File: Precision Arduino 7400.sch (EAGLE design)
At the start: 165 parts, among them U001 74HC4017, U002 74LVC14A, U010 74HC4017, U035 74LVC14A, U101 74HC4017, U110 74HC4017, U201 5319, U401 ATMEGA32U4QFN2, Y401 16MHz

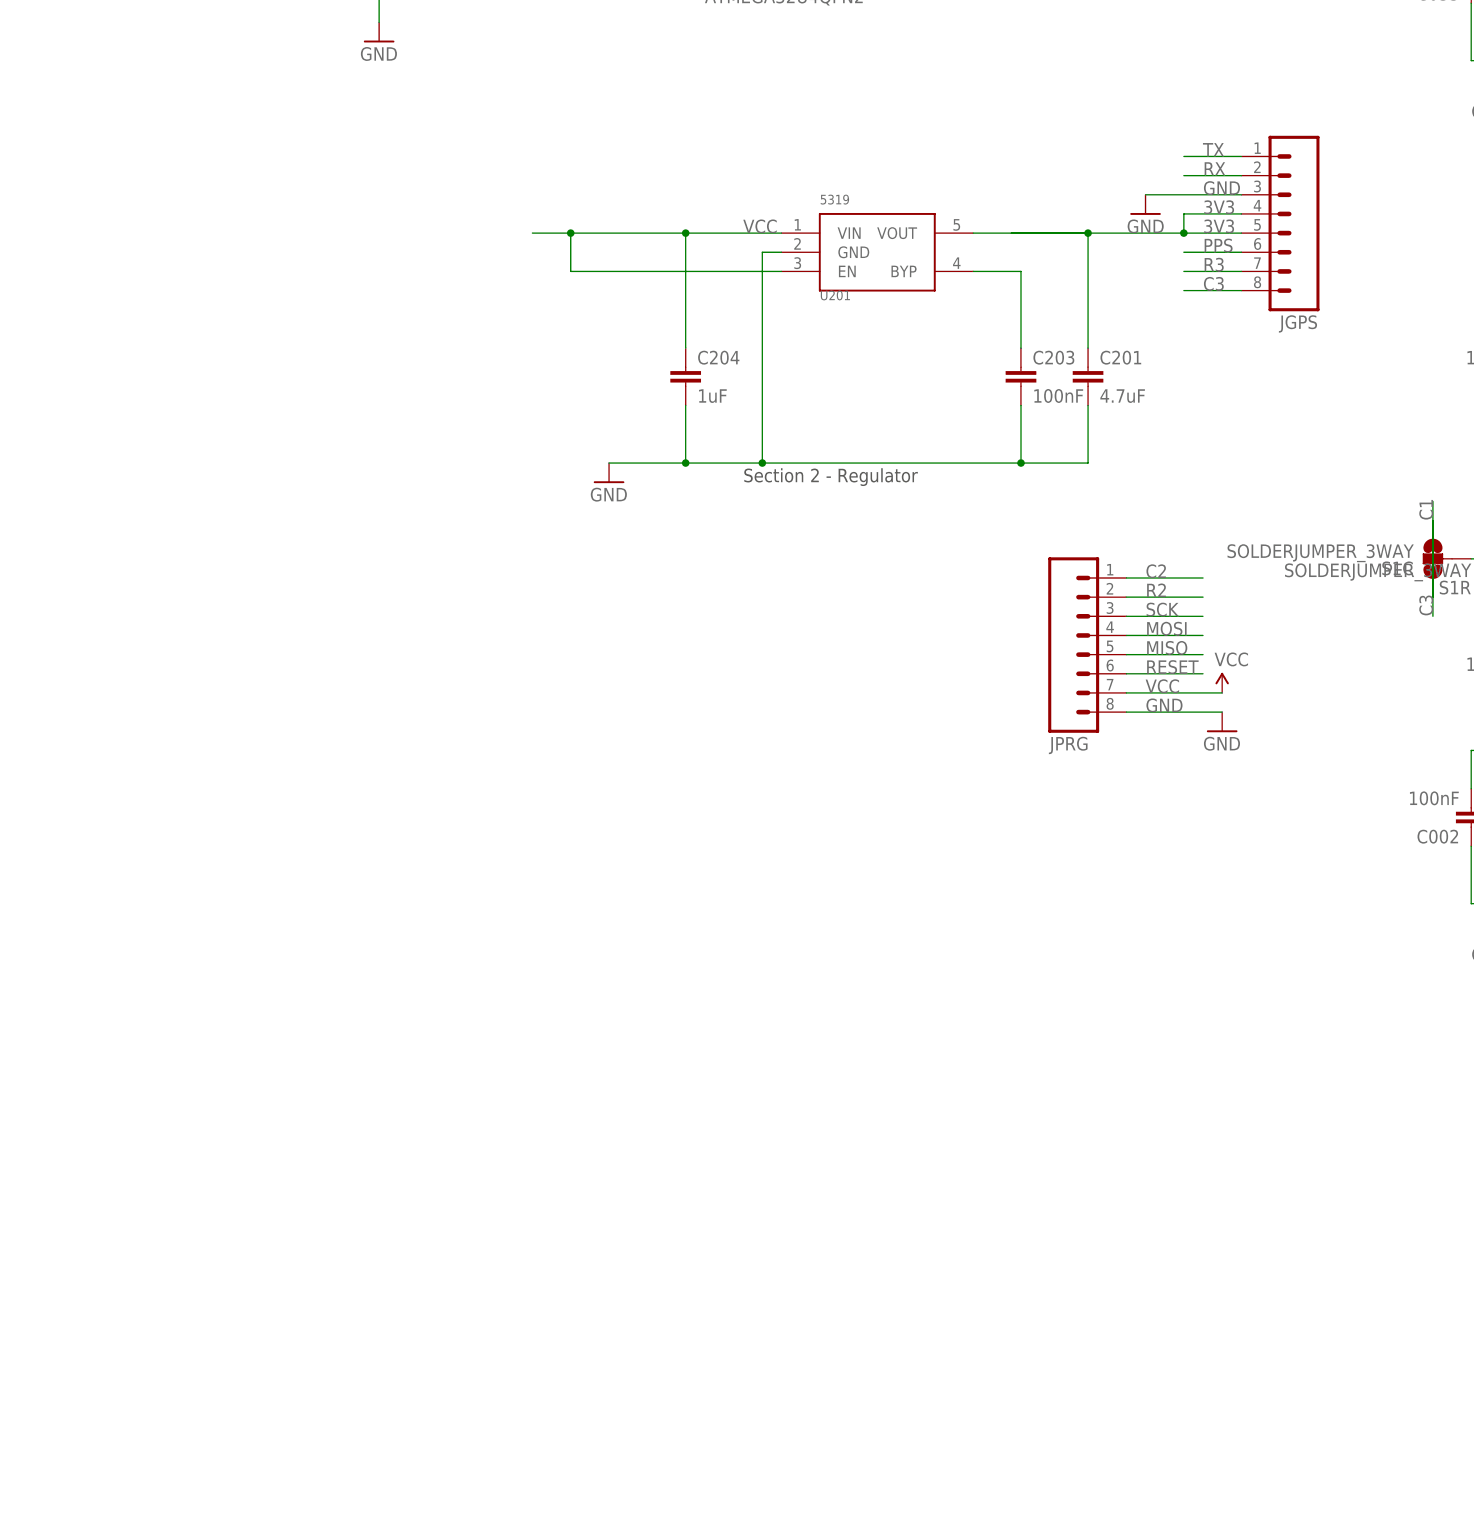
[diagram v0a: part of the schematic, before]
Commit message: Finished connecting hands, ripped up the rest of thw wires
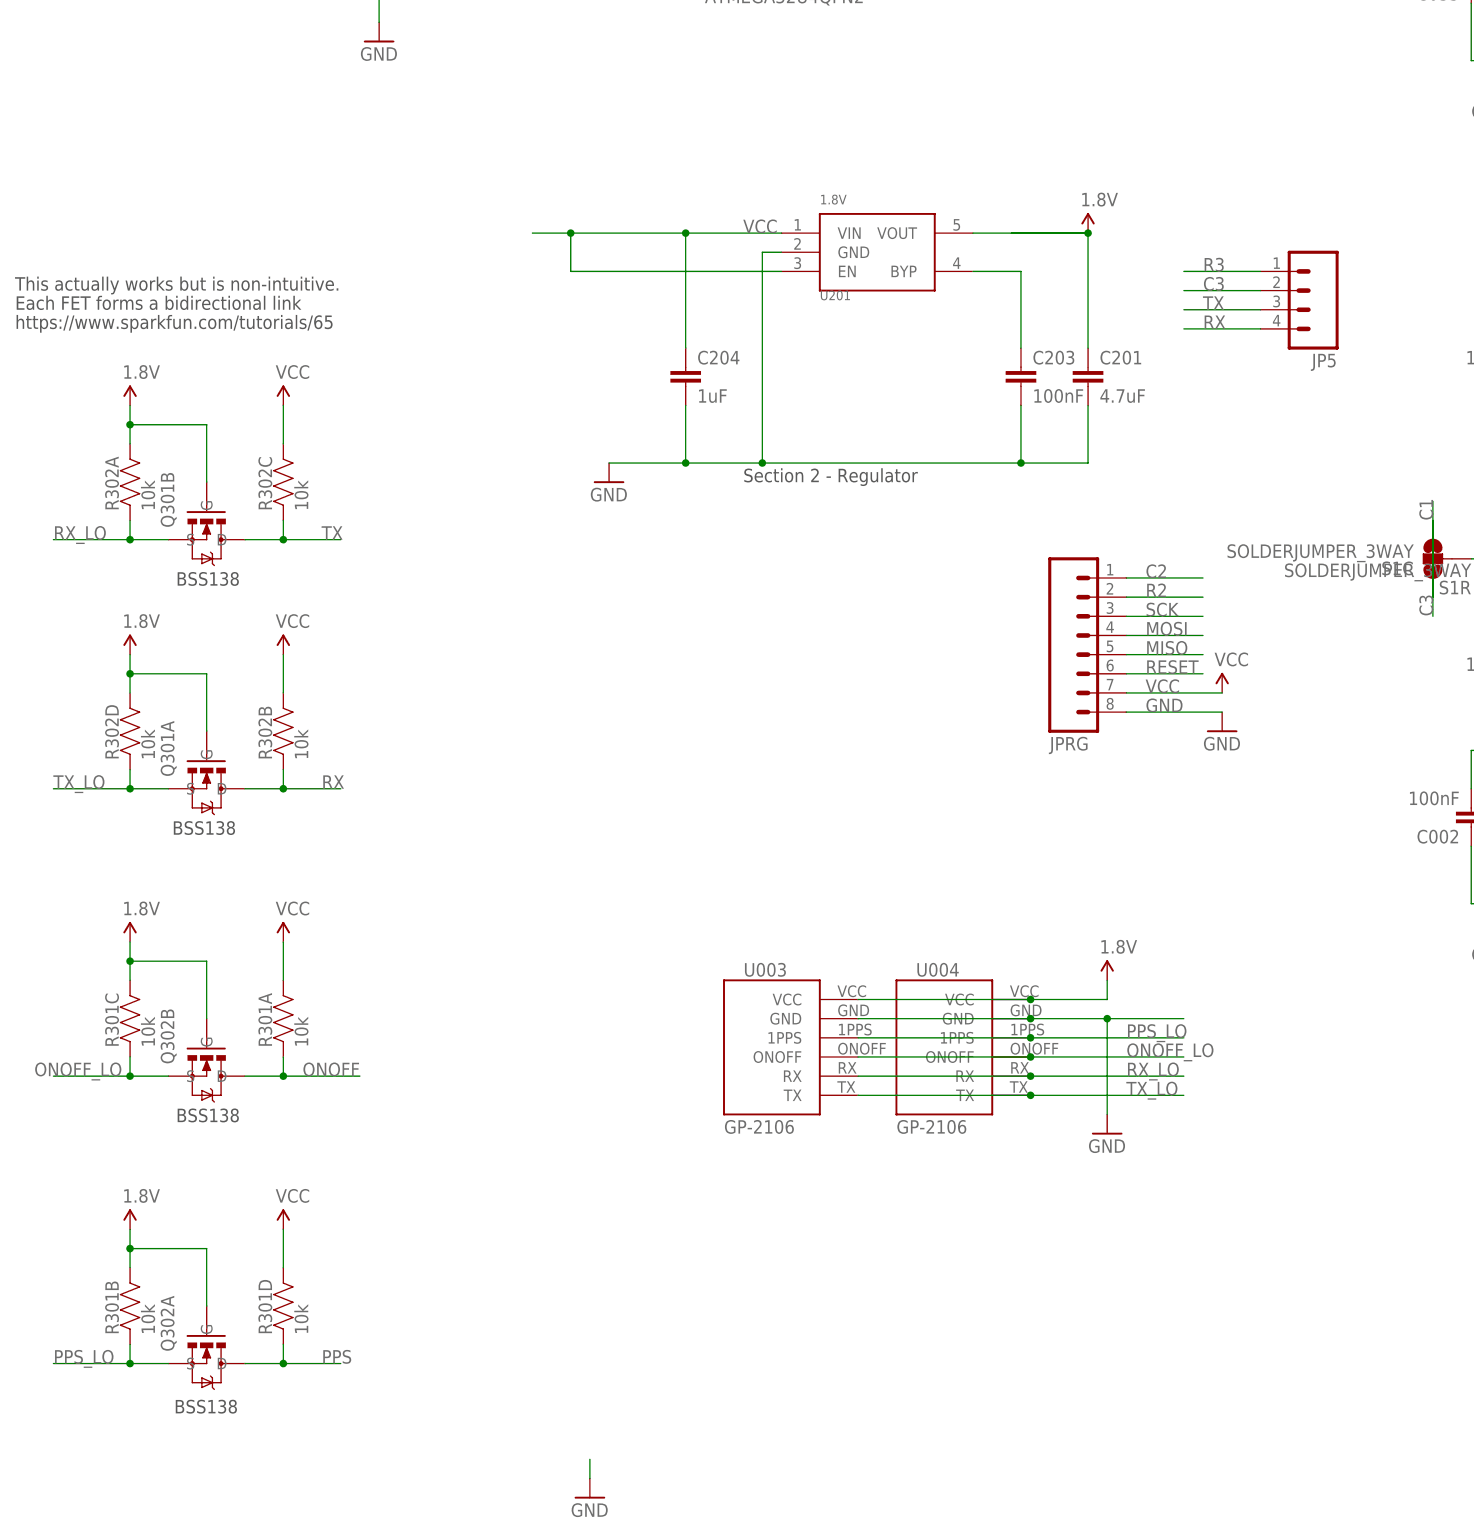
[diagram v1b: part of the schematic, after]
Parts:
- removed JGPS: (no value), SparkFun-Connectors:M081X08
- added JP5: (no value), SparkFun-Connectors:M04PTH
- added Q301, Q302: BSS138DW, KwanSystems:BSS138DW
- added R301, R302: 10k, KwanSystems:RP404
- added U003, U004: GP-2106, SparkFun:GP-2106
- U201: value 5319 -> 1.8V
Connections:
- removed net 3V3: C201.1, JGPS.4, JGPS.5, U201.VOUT
- new net 1.8V: C201.1, Q301A.G, Q301B.G, Q302A.G, Q302B.G, R301B.2, R301C.2, R302A.2, R302D.2, U003.VCC, U004.VCC, U201.VOUT
- new net ONOFF: Q302B.D, R301A.1
- new net ONOFF_LO: Q302B.S, R301C.1, U003.ONOFF, U004.ONOFF
- new net PPS_LO: Q302A.S, R301B.1, U003.1PPS, U004.1PPS
- new net RX_LO: Q301B.S, R302A.1, U003.RX, U004.RX
- new net TX_LO: Q301A.S, R302D.1, U003.TX, U004.TX
- net C3: now also JP5.2; no longer JGPS.8
- net GND: now also U003.GND, U004.GND; no longer JGPS.3
- net PPS: now also Q302A.D, R301D.1; no longer JGPS.6
- net R3: now also JP5.1; no longer JGPS.7
- net RX: now also JP5.4, Q301A.D, R302B.1; no longer JGPS.2
- net TX: now also JP5.3, Q301B.D, R302C.1; no longer JGPS.1
- net VCC: now also R301A.2, R301D.2, R302B.2, R302C.2
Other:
- note added: "BSS138"
- note added: "Each FET forms a bidirectional link"
- note added: "This actually works but is non-intuitive."
- note added: "https://www.sparkfun.com/tutorials/65"

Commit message: Rewired the left side 3-5 gates
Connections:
- net P03X: now also U035F.A; no longer U035C.A
- net P04X: now also U035C.A; no longer U035F.A
- net P05X: now also U035A.A; no longer U035D.A
- net P13X: now also U035E.A; no longer U035B.A
- net P14X: now also U035D.A; no longer U035A.A
- net P15X: now also U035B.A; no longer U035E.A
- net Q03X: now also U035F.Y; no longer U035C.Y
- net Q04X: now also U035C.Y; no longer U035F.Y
- net Q05X: now also U035A.Y; no longer U035D.Y
- net Q13X: now also U035E.Y; no longer U035B.Y
- net Q14X: now also U035D.Y; no longer U035A.Y
- net Q15X: now also U035B.Y; no longer U035E.Y
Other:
- moved on the sheet: U035A, U035B, U035C, U035D, U035E, U035F
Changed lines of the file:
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@@
 <instance part="U001" gate="G$1" x="7.62" y="58.42"/>
 <instance part="U010" gate="G$1" x="7.62" y="17.78"/>
-<instance part="U035" gate="E" x="50.8" y="-144.78"/>
-<instance part="U035" gate="B" x="50.8" y="-119.38"/>
-<instance part="U035" gate="A" x="50.8" y="-132.08"/>
-<instance part="U035" gate="C" x="50.8" y="-7.62"/>
-<instance part="U035" gate="F" x="50.8" y="-20.32"/>
-<instance part="U035" gate="D" x="50.8" y="-33.02"/>
+<instance part="U035" gate="B" x="50.8" y="-144.78"/>
+<instance part="U035" gate="E" x="50.8" y="-119.38"/>
+<instance part="U035" gate="D" x="50.8" y="-132.08"/>
+<instance part="U035" gate="F" x="50.8" y="-7.62"/>
+<instance part="U035" gate="C" x="50.8" y="-20.32"/>
+<instance part="U035" gate="A" x="50.8" y="-33.02"/>
 <instance part="U035" gate="G$1" x="-17.78" y="12.7"/>
 <instance part="D000" gate="G$1" x="93.98" y="38.1" smashed="yes">
@@
 <wire x1="35.56" y1="22.86" x2="35.56" y2="-7.62" width="0.1524" layer="91"/>
 <wire x1="35.56" y1="-7.62" x2="40.64" y2="-7.62" width="0.1524" layer="91"/>
-<pinref part="U035" gate="C" pin="A"/>
+<pinref part="U035" gate="F" pin="A"/>
 <label x="22.86" y="22.86" size="1.778" layer="95"/>
 </segment>
@@
 <wire x1="20.32" y1="20.32" x2="33.02" y2="20.32" width="0.1524" layer="91"/>
 <wire x1="33.02" y1="20.32" x2="33.02" y2="-20.32" width="0.1524" layer="91"/>
-<pinref part="U035" gate="F" pin="A"/>
+<pinref part="U035" gate="C" pin="A"/>
 <wire x1="33.02" y1="-20.32" x2="40.64" y2="-20.32" width="0.1524" layer="91"/>
 <label x="22.86" y="20.32" size="1.778" layer="95"/>
@@
 <wire x1="20.32" y1="17.78" x2="30.48" y2="17.78" width="0.1524" layer="91"/>
 <wire x1="30.48" y1="17.78" x2="30.48" y2="-33.02" width="0.1524" layer="91"/>
-<pinref part="U035" gate="D" pin="A"/>
+<pinref part="U035" gate="A" pin="A"/>
 <wire x1="30.48" y1="-33.02" x2="40.64" y2="-33.02" width="0.1524" layer="91"/>
 <label x="22.86" y="17.78" size="1.778" layer="95"/>
@@
 <net name="Q03X" class="0">
 <segment>
-<pinref part="U035" gate="C" pin="Y"/>
+<pinref part="U035" gate="F" pin="Y"/>
 <wire x1="60.96" y1="-7.62" x2="66.04" y2="-7.62" width="0.1524" layer="91"/>
 <label x="60.96" y="-7.62" size="1.778" layer="95"/>
@@
 <net name="Q04X" class="0">
 <segment>
-<pinref part="U035" gate="F" pin="Y"/>
+<pinref part="U035" gate="C" pin="Y"/>
 <wire x1="60.96" y1="-20.32" x2="66.04" y2="-20.32" width="0.1524" layer="91"/>
 <label x="60.96" y="-20.32" size="1.778" layer="95"/>
@@
 <net name="Q05X" class="0">
 <segment>
-<pinref part="U035" gate="D" pin="Y"/>
+<pinref part="U035" gate="A" pin="Y"/>
 <wire x1="60.96" y1="-33.02" x2="66.04" y2="-33.02" width="0.1524" layer="91"/>
 <label x="60.96" y="-33.02" size="1.778" layer="95"/>
@@
 <wire x1="35.56" y1="-88.9" x2="35.56" y2="-119.38" width="0.1524" layer="91"/>
 <label x="22.86" y="-88.9" size="1.778" layer="95"/>
-<pinref part="U035" gate="B" pin="A"/>
+<pinref part="U035" gate="E" pin="A"/>
 <wire x1="40.64" y1="-119.38" x2="35.56" y2="-119.38" width="0.1524" layer="91"/>
 </segment>
@@
 <wire x1="33.02" y1="-91.44" x2="33.02" y2="-132.08" width="0.1524" layer="91"/>
 <label x="22.86" y="-91.44" size="1.778" layer="95"/>
-<pinref part="U035" gate="A" pin="A"/>
+<pinref part="U035" gate="D" pin="A"/>
 <wire x1="40.64" y1="-132.08" x2="33.02" y2="-132.08" width="0.1524" layer="91"/>
 </segment>
@@
 <wire x1="30.48" y1="-93.98" x2="30.48" y2="-144.78" width="0.1524" layer="91"/>
 <label x="22.86" y="-93.98" size="1.778" layer="95"/>
-<pinref part="U035" gate="E" pin="A"/>
+<pinref part="U035" gate="B" pin="A"/>
 <wire x1="40.64" y1="-144.78" x2="30.48" y2="-144.78" width="0.1524" layer="91"/>
 </segment>
@@
 <wire x1="60.96" y1="-119.38" x2="66.04" y2="-119.38" width="0.1524" layer="91"/>
 <label x="60.96" y="-119.38" size="1.778" layer="95"/>
-<pinref part="U035" gate="B" pin="Y"/>
+<pinref part="U035" gate="E" pin="Y"/>
 <pinref part="R350" gate="C" pin="1"/>
 </segment>
@@
 <wire x1="60.96" y1="-132.08" x2="66.04" y2="-132.08" width="0.1524" layer="91"/>
 <label x="60.96" y="-132.08" size="1.778" layer="95"/>
-<pinref part="U035" gate="A" pin="Y"/>
+<pinref part="U035" gate="D" pin="Y"/>
 <pinref part="R350" gate="D" pin="1"/>
 </segment>
@@
 <wire x1="60.96" y1="-144.78" x2="66.04" y2="-144.78" width="0.1524" layer="91"/>
 <label x="60.96" y="-144.78" size="1.778" layer="95"/>
-<pinref part="U035" gate="E" pin="Y"/>
+<pinref part="U035" gate="B" pin="Y"/>
 <pinref part="R351" gate="B" pin="1"/>
 </segment>
